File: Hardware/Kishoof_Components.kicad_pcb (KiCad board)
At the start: 4 copper layers, 70.8 x 110 mm, 120 parts, among them J1 SWD_Header, J10 VOct, J11 WavetablePosA, J12 WavetablePos, J13 VCA, J18 USB_C_Receptacle, J2 Eurorack_10_pin_power, J3 Conn_01x02_Pin, J4 Conn_01x01_Socket, J7 Audio_Out_L, J8 Audio_Out_R, J9 WarpCV, SW1 Encoder, SW2 Mode_Switch, SW3 Octave_Switch, SW4 ChB_Output, SW5 SW_Push, U1 STM32H7B0VBTx, U2 PCM5100APW, U3 TPS561201, U4 LT1117-3.3, U5 MCP6002, U6 MX25LM51245G, U7 MCP6004, U8 TL072, U9 STF202-22T1G, Y1 8MHz 20pF

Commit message: Updating JLC assembly part number
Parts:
- C23: value 10nF -> 100nF
- R12, R17, R20, R23, R26: value 91k -> 82k
- R33: value 47k -> 33k
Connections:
- R25 pad 2: /-5V_REF -> unconnected-(R25-Pad2)
- R26 pad 2: /VCA_CV -> unconnected-(R26-Pad2)
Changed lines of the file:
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@@
 	(net 140 "unconnected-(U1-PD10-Pad57)")
 	(net 141 "/B_Octave_Btn")
+	(net 142 "unconnected-(R25-Pad2)")
+	(net 143 "unconnected-(R26-Pad2)")
 	(footprint "Custom_Footprints:THONKICONN_hole"
 		(locked yes)
@@
 			(layers "B.Cu" "B.Paste" "B.Mask")
 			(roundrect_rratio 0.25)
-			(net 80 "/-5V_REF")
+			(net 142 "unconnected-(R25-Pad2)")
 			(pintype "passive")
 		)
@@
 			)
 		)
+		(property "Part_Number" "C4190"
+			(at 0 0 180)
+			(unlocked yes)
+			(layer "B.Fab")
+			(hide yes)
+			(effects
+				(font
+					(size 1 1)
+					(thickness 0.15)
+				)
+				(justify mirror)
+			)
+		)
 		(property ki_fp_filters "R_*")
 		(sheetname "Root")
@@
 			)
 		)
+		(property "Part_Number" "C25819"
+			(at 0 0 180)
+			(unlocked yes)
+			(layer "B.Fab")
+			(hide yes)
+			(effects
+				(font
+					(size 1 1)
+					(thickness 0.15)
+				)
+				(justify mirror)
+			)
+		)
 		(property ki_fp_filters "R_*")
 		(sheetname "Root")
@@
 			)
 		)
-		(property "Value" "91k"
+		(property "Value" "82k"
 			(at 0 -1.43 -90)
 			(layer "B.Fab")
@@
 			)
 		)
-		(property "Value" "91k"
+		(property "Value" "82k"
 			(at 0 -1.43 0)
 			(layer "B.Fab")
@@
 			)
 		)
+		(property "Part_Number" " C8598"
+			(at 0 0 0)
+			(unlocked yes)
+			(layer "B.Fab")
+			(hide yes)
+			(effects
+				(font
+					(size 1 1)
+					(thickness 0.15)
+				)
+				(justify mirror)
+			)
+		)
 		(property ki_fp_filters "TO-???* *_Diode_* *SingleDiode* D_*")
 		(sheetname "Root")
@@
 			)
 		)
+		(property "Part_Number" "C6961"
+			(at 0 0 0)
+			(unlocked yes)
+			(layer "B.Fab")
+			(hide yes)
+			(effects
+				(font
+					(size 1 1)
+					(thickness 0.15)
+				)
+				(justify mirror)
+			)
+		)
 		(property ki_fp_filters "SOIC*3.9x4.9mm*P1.27mm* DIP*W7.62mm* TO*99* OnSemi*Micro8* TSSOP*3x3mm*P0.65mm* TSSOP*4.4x3mm*P0.65mm* MSOP*3x3mm*P0.65mm* SSOP*3.9x4.9mm*P0.635mm* LFCSP*2x2mm*P0.5mm* *SIP* SOIC*5.3x6.2mm*P1.27mm*")
 		(sheetname "Root")
@@
 			)
 		)
-		(property "Value" "91k"
+		(property "Value" "82k"
 			(at 0 -1.43 90)
 			(layer "B.Fab")
@@
 			)
 		)
-		(property "Part_Number" "C15849"
+		(property "Part_Number" "C23630"
 			(at 0 0 0)
 			(unlocked yes)
@@
 			)
 		)
-		(property "Part_Number" "C1588"
+		(property "Part_Number" "C1604"
 			(at 0 0 180)
 			(unlocked yes)
@@
 			)
 		)
-		(property "Value" "10nF"
+		(property "Value" "100nF"
 			(at 0 -1.43 180)
 			(layer "B.Fab")
@@
 			)
 		)
-		(property "Part_Number" "C1588"
+		(property "Part_Number" "C1604"
 			(at 0 0 0)
 			(unlocked yes)
@@
 			)
 		)
+		(property "Part_Number" "C25803"
+			(at 0 0 0)
+			(unlocked yes)
+			(layer "B.Fab")
+			(hide yes)
+			(effects
+				(font
+					(size 1 1)
+					(thickness 0.15)
+				)
+				(justify mirror)
+			)
+		)
 		(property ki_fp_filters "R_*")
 		(sheetname "Root")
@@
 			)
 		)
-		(property "Part_Number" "C1595"
+		(property "Part_Number" "C1604"
 			(at 0 0 -90)
 			(unlocked yes)
@@
 			)
 		)
+		(property "Part_Number" "C23186"
+			(at 0 0 90)
+			(unlocked yes)
+			(layer "B.Fab")
+			(hide yes)
+			(effects
+				(font
+					(size 1 1)
+					(thickness 0.15)
+				)
+				(justify mirror)
+			)
+		)
 		(property ki_fp_filters "R_*")
 		(sheetname "Root")
@@
 			)
 		)
-		(property "Part_Number" "C131154"
+		(property "Part_Number" ""
 			(at 0 0 180)
 			(unlocked yes)
@@
 			)
 		)
-		(property "Value" "91k"
+		(property "Value" "82k"
 			(at 0 -1.43 180)
 			(layer "B.Fab")
@@
 			)
 		)
+		(property "Part_Number" "C25804"
+			(at 0 0 0)
+			(unlocked yes)
+			(layer "B.Fab")
+			(hide yes)
+			(effects
+				(font
+					(size 1 1)
+					(thickness 0.15)
+				)
+				(justify mirror)
+			)
+		)
 		(property ki_fp_filters "R_*")
 		(sheetname "Root")
@@
 			)
 		)
+		(property "Part_Number" "C4190"
+			(at 0 0 0)
+			(unlocked yes)
+			(layer "B.Fab")
+			(hide yes)
+			(effects
+				(font
+					(size 1 1)
+					(thickness 0.15)
+				)
+				(justify mirror)
+			)
+		)
 		(property ki_fp_filters "R_*")
 		(sheetname "Root")
@@
 			)
 		)
-		(property "Part_Number" "C116668"
+		(property "Part_Number" ""
 			(at 0 0 0)
 			(unlocked yes)
@@
 			)
 		)
-		(property "Part_Number" "C15849"
+		(property "Part_Number" "C23630"
 			(at 0 0 90)
 			(unlocked yes)
@@
 			)
 		)
-		(property "Part_Number" "C23206"
+		(property "Part_Number" "C25819"
 			(at 0 0 180)
 			(unlocked yes)
@@
 			)
 		)
-		(property "Value" "91k"
+		(property "Value" "82k"
 			(at 0 -1.43 180)
 			(layer "B.Fab")
@@
 			(layers "B.Cu" "B.Paste" "B.Mask")
 			(roundrect_rratio 0.25)
-			(net 25 "/VCA_CV")
+			(net 143 "unconnected-(R26-Pad2)")
 			(pintype "passive")
 		)
@@
 			)
 		)
-		(property "Part_Number" "C1595"
+		(property "Part_Number" "C1604"
 			(at 0 0 0)
 			(unlocked yes)
@@
 			)
 		)
-		(property "Value" "47k"
+		(property "Value" "33k"
 			(at 0 -1.43 0)
 			(layer "B.Fab")
@@
 			)
 		)
+		(property "Part_Number" "C4190"
+			(at 0 0 180)
+			(unlocked yes)
+			(layer "B.Fab")
+			(hide yes)
+			(effects
+				(font
+					(size 1 1)
+					(thickness 0.15)
+				)
+				(justify mirror)
+			)
+		)
 		(property ki_fp_filters "R_*")
 		(sheetname "Root")
@@
 			)
 		)
-		(property "Part_Number" "C57112"
+		(property "Part_Number" "C14663"
 			(at 0 0 -90)
 			(unlocked yes)
@@
 			)
 		)
+		(property "Part_Number" "C23345"
+			(at 0 0 180)
+			(unlocked yes)
+			(layer "B.Fab")
+			(hide yes)
+			(effects
+				(font
+					(size 1 1)
+					(thickness 0.15)
+				)
+				(justify mirror)
+			)
+		)
 		(property ki_fp_filters "R_*")
 		(sheetname "Root")
@@
 			)
 		)
+		(property "Part_Number" "C23186"
+			(at 0 0 90)
+			(unlocked yes)
+			(layer "B.Fab")
+			(hide yes)
+			(effects
+				(font
+					(size 1 1)
+					(thickness 0.15)
+				)
+				(justify mirror)
+			)
+		)
 		(property ki_fp_filters "R_*")
 		(sheetname "Root")
@@
 			)
 		)
+		(property "Part_Number" " C8598"
+			(at 0 0 0)
+			(unlocked yes)
+			(layer "B.Fab")
+			(hide yes)
+			(effects
+				(font
+					(size 1 1)
+					(thickness 0.15)
+				)
+				(justify mirror)
+			)
+		)
 		(property ki_fp_filters "TO-???* *_Diode_* *SingleDiode* D_*")
 		(sheetname "Root")
@@
 			)
 		)
-		(property "Part_Number" "C326343"
+		(property "Part_Number" ""
 			(at 0 0 180)
 			(unlocked yes)

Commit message: Schematic Clean up
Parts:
- J4: renamed from J12; value WavetablePos -> WavetablePosB
- renumbered J18 to J10, J3 to J11, J4 to J12, J11 to J3, J9 to J5, J10 to J6, J13 to J7, J7 to J8, J8 to J9, SW5 to SW1, SW1 to SW5, WarpAmtTrm2 to WarpAmtTrm1
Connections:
- net /AUDIO_OUT_L renamed Audio_Out_L
- net /AUDIO_OUT_R renamed Audio_Out_R
- net /AudioIn renamed AudioIn
- net /B_Octave_Btn renamed B_Octave_Btn
- net /ChB_Mix renamed ChB_Mix
- net /ChB_RM renamed ChB_RM
- net /ENCODER_BTN renamed Encoder_Btn
- net /ENCODER_DN renamed Encoder_Down
- net /ENCODER_UP renamed Encoder_Up
- net /EXT_AUDIO_IN renamed Ext_Audio_In
- net /LCD_BACKLIGHT renamed LCD_Backlight
- net /LCD_DC renamed LCD_DC
- net /LCD_RESET renamed LCD_RESET
- net /LCD_SPI3_MOSI renamed LCD_SPI3_MOSI
- net /LCD_SPI3_SCK renamed LCD_SPI3_SCK
- net /LCD_SPI3_SS renamed LCD_SPI3_SS
- net /LED_B_Oct renamed /LED_Oct_B
- net /LED_OCT_B renamed LED_Oct_B_Out
- net /Mode renamed Mode
- net /Octave_Down renamed Octave_Down
- net /Octave_Up renamed Octave_Up
- net /PITCH_CV renamed Pitch_CV_In
- net /Pitch_CV_Scaled renamed Pitch_CV_Scaled
- net /UART_RX renamed UART_RX
- net /UART_TX renamed UART_TX
- net /USB_D+ renamed USB_D+
- net /USB_D- renamed USB_D-
- net /USB_DM renamed USB_DM
- net /USB_DP renamed USB_DP
- net /USB_VBUS renamed USB_VBUS
- net /VcaCV renamed VcaCV
- net /WARP_AMT_POT renamed Warp_Amt_Pot
- net /WARP_AMT_TRM renamed Warp_Amt_Trm
- net /WARP_CV renamed Warp_CV_In
- net /WAVETABLE_POS_A_CV renamed Wavetable_Pos_A_CV_In
- net /WAVETABLE_POS_A_POT renamed Wavetable_Pos_A_Pot
- net /WAVETABLE_POS_A_TRM renamed Wavetable_Pos_A_Trm
- net /WAVETABLE_POS_B_CV renamed Wavetable_Pos_B_CV_In
- net /WAVETABLE_POS_B_POT renamed Wavetable_Pos_B_Pot
- net /WarpCV renamed WarpCV
- net /Warp_Polarity_Btn renamed Warp_Polarity_Btn
- net /Warp_Type_Pot renamed Warp_Type_Pot
- net /WavetablePosB_CV renamed WavetablePosB_CV
- J7 pad 3: /VCA_CV -> VCA_CV_In
- R25 pad 2: unconnected-(R25-Pad2) -> /-5V_REF
- R26 pad 2: unconnected-(R26-Pad2) -> VCA_CV_In
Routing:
- net VCA_CV_In: track 0.00 -> 60.0 mm
- net /VCA_CV: track 60.0 -> 0.00 mm

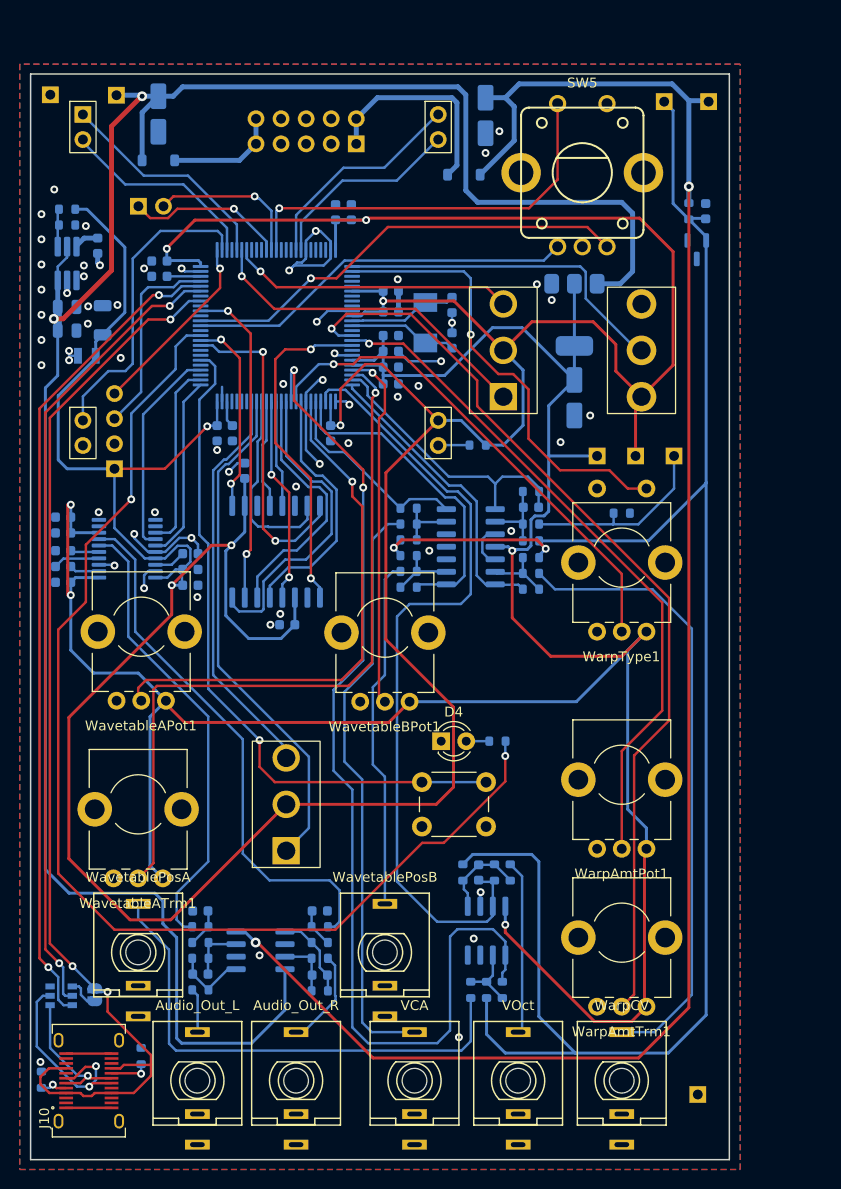
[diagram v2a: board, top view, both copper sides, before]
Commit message: Separated PCB controls and components
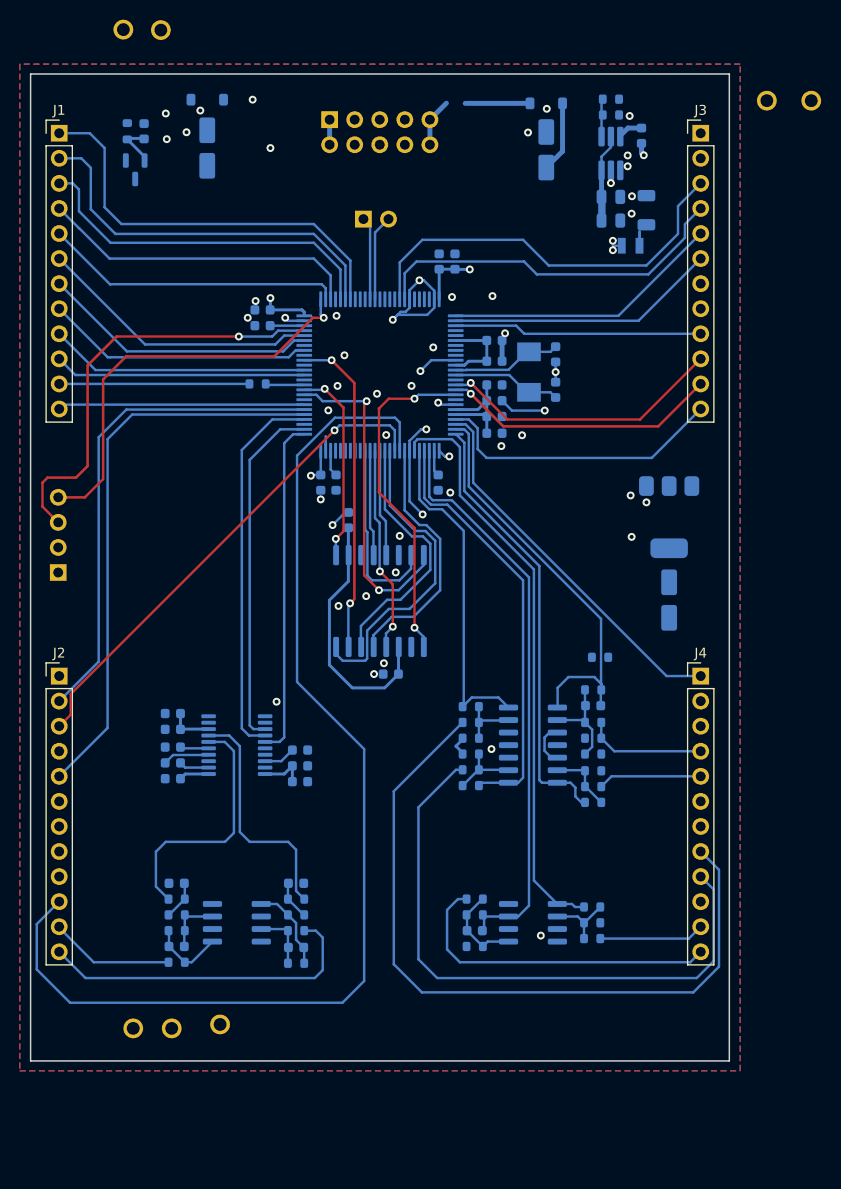
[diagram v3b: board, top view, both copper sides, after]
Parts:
- removed D4: LED_Small, LED_THT:LED_D3.0mm_FlatTop
- removed J10: USB_C_Receptacle, Custom_Footprints:USB_C_Receptacle_Amphenol_12401951E412A
- removed J11: Conn_01x02_Pin, Connector_PinHeader_2.54mm:PinHeader_1x02_P2.54mm_Vertical
- removed J12: Conn_01x01_Socket, Connector_PinHeader_2.54mm:PinHeader_1x01_P2.54mm_Vertical
- removed the J5 at (115.0, 141.0)
- removed the J6 at (104.5, 141.0)
- removed J8: Audio_Out_L, Custom_Footprints:THONKICONN_hole
- removed J9: Audio_Out_R, Custom_Footprints:THONKICONN_hole
- removed JP1: Jumper, Jumper:SolderJumper-2_P1.3mm_Open_RoundedPad1.0x1.5mm
- removed R28, R29: 5k1, Resistor_SMD:R_0603_1608Metric
- removed SW1: SW_Push, Custom_Footprints:SW_PUSH_6mm_aligned
- removed SW2: Mode_Switch, Custom_Footprints:SPDT_Miniature
- removed SW3: Octave_Switch, Custom_Footprints:SP3T_Mini_Switch
- removed SW4: ChB_Output, Custom_Footprints:SP3T_Mini_Switch
- removed SW5: Encoder, Custom_Footprints:Encoder
- removed U10: ~, Custom_Footprints:LCD_Riser
- removed U9: STF202-22T1G, Custom_Footprints:STF202-22T1G
- removed WarpAmtPot1, WarpAmtTrm1, WavetableAPot1, WavetableATrm1, WavetableBPot1: B10k, Custom_Footprints:Alpha_9mm_Potentiometer_Aligned
- removed WarpType1: WarpTypePot, Custom_Footprints:Bourns_Switch_Potentiometer
- added J1: Conn_01x12_Pin, Connector_PinHeader_2.54mm:PinHeader_1x12_P2.54mm_Vertical, F.Cu at (58.0, 45.0)
- added J2: Conn_01x12_Pin, Connector_PinHeader_2.54mm:PinHeader_1x12_P2.54mm_Vertical, F.Cu at (58.0, 100.0)
- J3: value WavetablePosA -> Conn_01x12_Pin; footprint Custom_Footprints:THONKICONN_hole -> Connector_PinHeader_2.54mm:PinHeader_1x12_P2.54mm_Vertical
- J4: value WavetablePosB -> Conn_01x12_Pin; footprint Custom_Footprints:THONKICONN_hole -> Connector_PinHeader_2.54mm:PinHeader_1x12_P2.54mm_Vertical
- J7: value VCA -> Conn_01x02_Pin; footprint Custom_Footprints:THONKICONN_hole -> Connector_PinHeader_2.54mm:PinHeader_1x02_P2.54mm_Vertical; moved to B.Cu
- TP2, TP3, TP4, TP5, TP6, TP7, TP8: footprint Connector_PinSocket_2.54mm:PinSocket_1x01_P2.54mm_Vertical -> Custom_Footprints:1.3mm_Test_Point
- moved J3 100.7 mm to (123.0, 45.0)
- moved J7 87.5 mm to (88.8, 53.7), turned to -90 degrees
- moved TP5 74.7 mm to (69.4, 135.7)
- moved TP6 74.7 mm to (65.5, 135.7)
- moved C36 57.5 mm to (66.6, 44.8)
- moved D3 57.5 mm to (65.7, 48.7)
- moved R14 57.5 mm to (64.9, 44.8)
- moved C6 56.2 mm to (113.9, 51.5)
- moved C7 56.2 mm to (113.9, 53.9)
- moved L2 56.2 mm to (115.9, 56.4)
- moved R1 56.2 mm to (113.9, 41.5)
- moved R2 56.2 mm to (113.9, 43.1)
- moved U3 56.2 mm to (113.9, 47.0)
- moved C8 56.2 mm to (117.0, 45.2)
- moved C9 56.2 mm to (117.5, 52.8)
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- renumbered J2 to J5, J1 to J6
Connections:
- net AudioIn renamed /AudioIn
- net Pitch_CV_Scaled renamed /Pitch_CV_Scaled
- net VcaCV renamed /VcaCV
- net WarpCV renamed /WarpCV
- net WavetablePosB_CV renamed /WavetablePosB_CV
- J3 pad 1: GND -> unconnected-(J3-Pin_1-Pad1)
- J3 pad 2: GND -> unconnected-(J3-Pin_2-Pad2)
- J3 pad 3: Wavetable_Pos_A_CV_In -> /LCD_DC
- J4 pad 1: GND -> /Wavetable_Pos_A_Trm
- J4 pad 2: GND -> unconnected-(J4-Pin_2-Pad2)
- J4 pad 3: Wavetable_Pos_B_CV_In -> /LCD_Backlight
- J7 pad 1: GND -> /UART_TX
- J7 pad 2: GND -> /UART_RX
- R10 pad 2: Audio_Out_R -> /Audio_Out_R
- R12 pad 2: Wavetable_Pos_B_CV_In -> /Wavetable_Pos_B_CV_In
- R15 pad 2: LCD_Backlight -> /LCD_Backlight
- R17 pad 2: Wavetable_Pos_A_CV_In -> /Wavetable_Pos_A_CV_In
- R20 pad 2: Warp_CV_In -> /Warp_CV_In
- R23 pad 2: Pitch_CV_In -> /Pitch_CV_In
- R26 pad 2: VCA_CV_In -> /VCA_CV_In
- R30 pad 2: LED_Oct_B_Out -> /LED_Oct_B_Out
- R31 pad 1: Ext_Audio_In -> /Ext_Audio_In
- R33 pad 2: Ext_Audio_In -> /Ext_Audio_In
- R9 pad 2: Audio_Out_L -> /Audio_Out_L
- U1 pad 1: Mode -> /Mode
- U1 pad 15: Warp_Amt_Trm -> /Warp_Amt_Trm
- U1 pad 16: Warp_Amt_Pot -> /Warp_Amt_Pot
- U1 pad 2: Warp_Polarity_Btn -> /Warp_Polarity_Btn
- U1 pad 22: Wavetable_Pos_B_Pot -> /Wavetable_Pos_B_Pot
- U1 pad 23: Wavetable_Pos_A_Trm -> /Wavetable_Pos_A_Trm
- U1 pad 3: unconnected-(U1-PE4-Pad3) -> /Encoder_Btn
- U1 pad 31: Wavetable_Pos_A_Pot -> /WavetablePosA_CV
- U1 pad 34: Warp_Type_Pot -> /Warp_Type_Pot
- U1 pad 35: /WavetablePosA_CV -> /Wavetable_Pos_A_Pot
- U1 pad 42: ChB_Mix -> unconnected-(U1-PE12-Pad42)
- U1 pad 43: ChB_RM -> unconnected-(U1-PE13-Pad43)
- U1 pad 55: unconnected-(U1-PD8-Pad55) -> /ChB_Mix
- U1 pad 56: B_Octave_Btn -> /ChB_RM
- U1 pad 57: unconnected-(U1-PD10-Pad57) -> /B_Octave_Btn
- U1 pad 63: Encoder_Up -> /Encoder_Up
- U1 pad 64: Encoder_Down -> /Encoder_Down
- U1 pad 68: USB_VBUS -> /USB_VBUS
- U1 pad 70: USB_DM -> /USB_DM
- U1 pad 71: USB_DP -> /USB_DP
- U1 pad 77: LCD_SPI3_SS -> /LCD_SPI3_SS
- U1 pad 78: LCD_SPI3_SCK -> /LCD_SPI3_SCK
- U1 pad 80: LCD_SPI3_MOSI -> /LCD_SPI3_MOSI
- U1 pad 81: Octave_Up -> /Octave_Up
- U1 pad 82: Octave_Down -> /Octave_Down
- U1 pad 86: UART_TX -> /UART_TX
- U1 pad 87: UART_RX -> /UART_RX
- U1 pad 88: Encoder_Btn -> unconnected-(U1-PD7-Pad88)
- U1 pad 92: LCD_DC -> /LCD_DC
- U1 pad 93: LCD_RESET -> /LCD_RESET
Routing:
- net +3.3V: track 400.5 -> 58.2 mm, vias 7 -> 3
- net +3.3VA: track 267.0 -> 19.5 mm, vias 4 -> 0
- net +12V: track 215.8 -> 15.7 mm, vias 2 -> 0
- net /-5V_REF: track 193.8 -> 6.91 mm, vias 2 -> 0
- net -12V: track 180.4 -> 0.00 mm, vias 2 -> 0
- net /LED_Oct_B: track 119.3 -> 3.94 mm, vias 2 -> 0
- net /Warp_Type_Pot: track 0.00 -> 114.4 mm
- net USB_VBUS: track 112.0 -> 0.00 mm, vias 3 -> 0
- net Warp_Amt_Trm: track 94.0 -> 0.00 mm, vias 1 -> 0
- net USB_DP: track 83.9 -> 0.00 mm, vias 2 -> 0
- net USB_DM: track 81.5 -> 0.00 mm, vias 2 -> 0
- net /VCA_CV_In: track 0.00 -> 75.0 mm
- net Wavetable_Pos_A_Trm: track 74.0 -> 0.00 mm, vias 1 -> 0
- net B_Octave_Btn: track 69.1 -> 0.00 mm, vias 1 -> 0
- net Warp_Amt_Pot: track 69.1 -> 0.00 mm, vias 1 -> 0
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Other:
- board size 70.8 x 110 mm -> 70.8 x 100 mm
- board text removed: "Ext"
